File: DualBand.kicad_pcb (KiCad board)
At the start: 2 copper layers, 74.3 x 57.2 mm, 47 parts, among them J1 Conn_01x02_Male, J2 Conn_01x03_Male, J3 Conn_01x01_Male, J4 Conn_01x10_Male, J5 Conn_01x03_Male, J6 Conn_01x10_Male, J7 Conn_01x03_Male, P2 AD8402ARUZ1, SW1 SW_Push, U1 LM7322QMAX/NOPB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

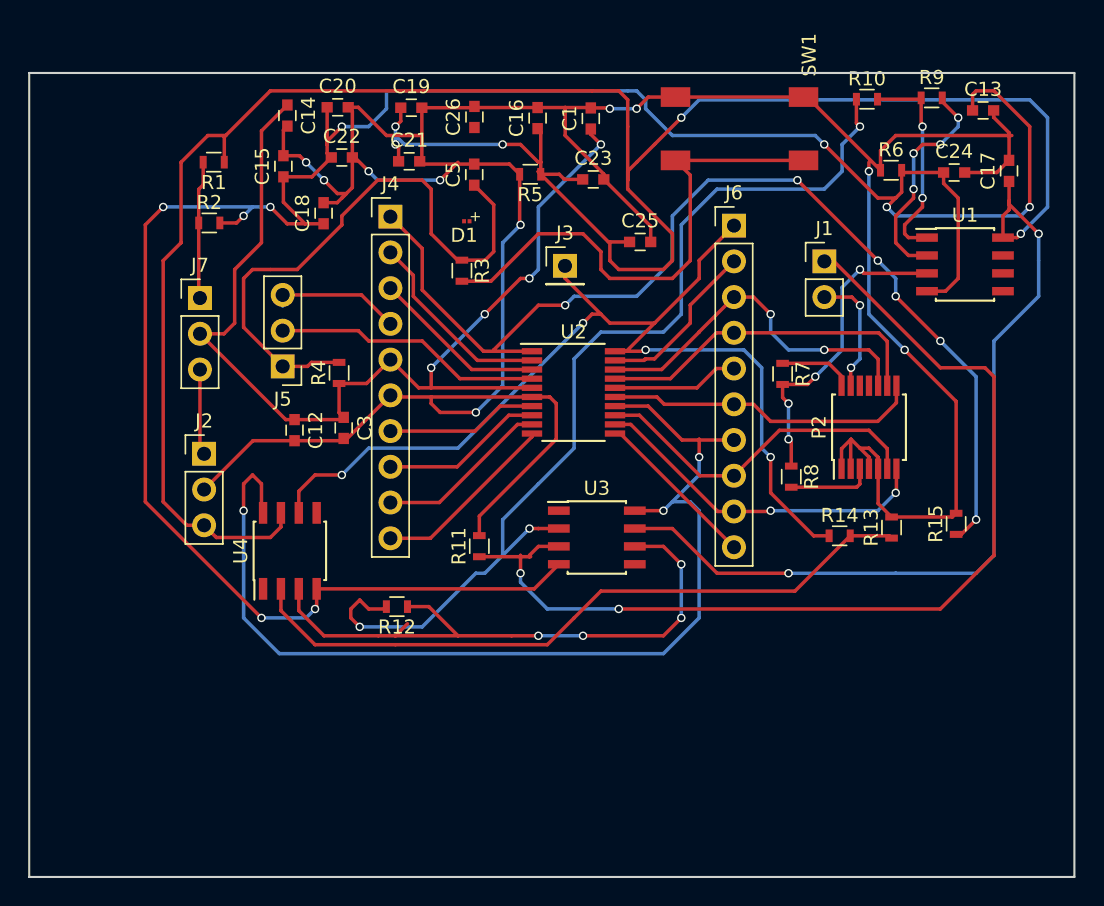
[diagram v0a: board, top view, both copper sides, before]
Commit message: Fixed the PCB edges so they're not enormous
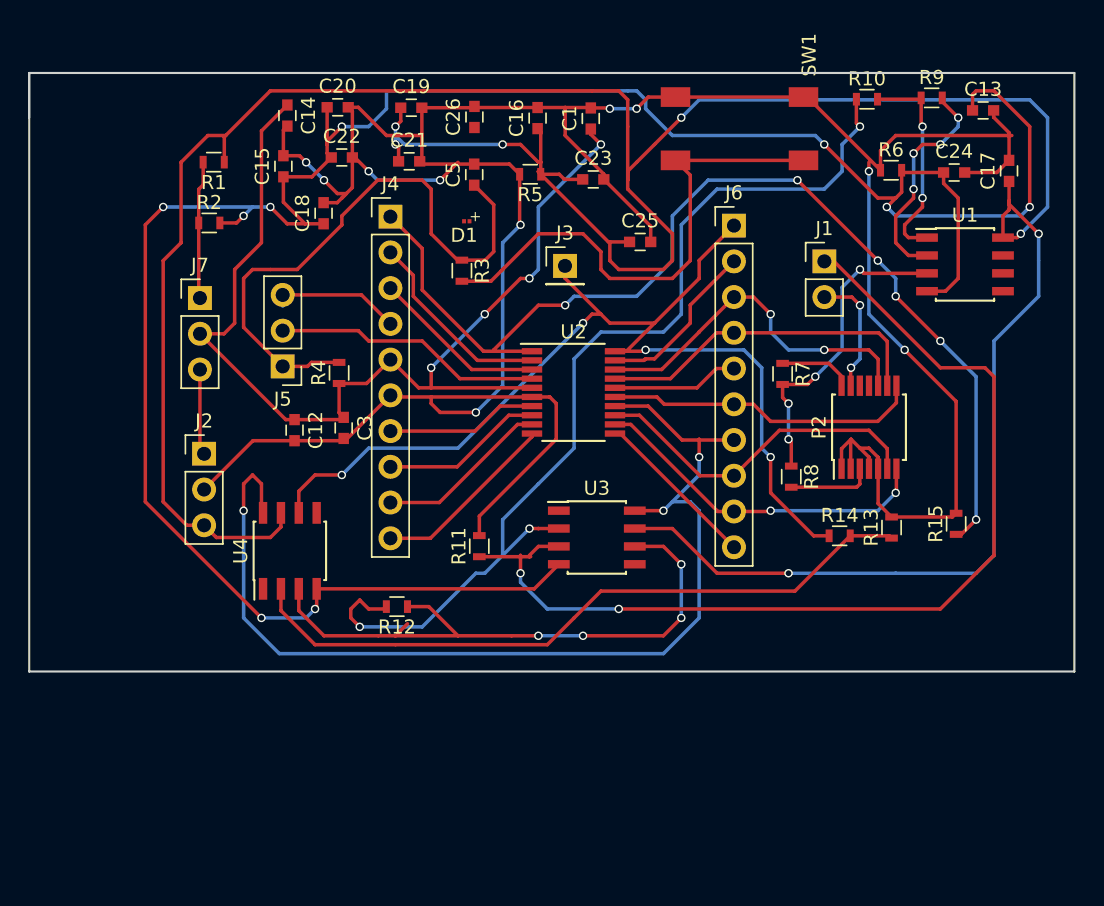
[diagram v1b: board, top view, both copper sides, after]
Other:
- board size 74.3 x 57.2 mm -> 74.3 x 42.5 mm
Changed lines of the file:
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@@
     (area 97.714999 97.953689 172.160001 167.8)
     (thickness 1.6)
-    (drawings 5)
+    (drawings 6)
     (tracks 642)
     (zones 0)
@@
     )
   )
+  (gr_line (start 97.79 100.965) (end 97.79 104.14) (angle 90) (layer Edge.Cuts) (width 0.15))
+  (gr_line (start 97.79 143.51) (end 97.79 100.965) (angle 90) (layer Edge.Cuts) (width 0.15))
+  (gr_line (start 172.085 143.51) (end 97.79 143.51) (angle 90) (layer Edge.Cuts) (width 0.15))
+  (gr_line (start 172.085 100.965) (end 172.085 143.51) (angle 90) (layer Edge.Cuts) (width 0.15))
   (dimension 74.295 (width 0.3) (layer F.SilkS)
     (gr_text "74.295 mm" (at 134.9375 166.449999) (layer F.SilkS)
@@
     (arrow2b (pts (xy 97.79 165.099999) (xy 98.916504 164.513578)))
   )
-  (gr_line (start 97.79 158.115) (end 97.79 100.965) (angle 90) (layer Edge.Cuts) (width 0.15))
-  (gr_line (start 172.085 158.115) (end 97.79 158.115) (angle 90) (layer Edge.Cuts) (width 0.15))
-  (gr_line (start 172.085 100.965) (end 172.085 158.115) (angle 90) (layer Edge.Cuts) (width 0.15))
   (gr_line (start 97.79 100.965) (end 172.085 100.965) (angle 90) (layer Edge.Cuts) (width 0.15))
-  (segment (start 163.679999 132.262618) (end 163.679999 124.309999) (width 0.25) (layer F.Cu) (net 1) (status 400000))
+  (segment (start 163.679999 132.262618) (end 163.679999 124.309999) (width 0.25) (layer F.Cu) (net 1))
   (segment (start 157.48 107.95) (end 157.48 107.315) (width 0.25) (layer F.Cu) (net 1))
   (via (at 157.48 107.95) (size 0.6) (drill 0.4) (layers F.Cu B.Cu) (net 1))
@@
   (segment (start 170.18 104.14) (end 168.91 102.87) (width 0.25) (layer B.Cu) (net 5))
   (segment (start 140.97 107.315) (end 142.24 106.045) (width 0.25) (layer F.Cu) (net 5))
-  (segment (start 168.002501 112.667499) (end 167.009882 112.667499) (width 0.25) (layer F.Cu) (net 5) (status 800000))
+  (segment (start 168.002501 112.667499) (end 167.009882 112.667499) (width 0.25) (layer F.Cu) (net 5))
   (segment (start 168.275 112.395) (end 168.002501 112.667499) (width 0.25) (layer F.Cu) (net 5))
   (via (at 168.275 112.395) (size 0.6) (drill 0.4) (layers F.Cu B.Cu) (net 5))
